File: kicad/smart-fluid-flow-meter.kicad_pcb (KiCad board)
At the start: 2 copper layers, 64 x 54 mm, 14 parts, among them J1 YF-S201, J2 Barrel_Jack, SW1 Factory reset button, U2 ESP32-DevkitV1

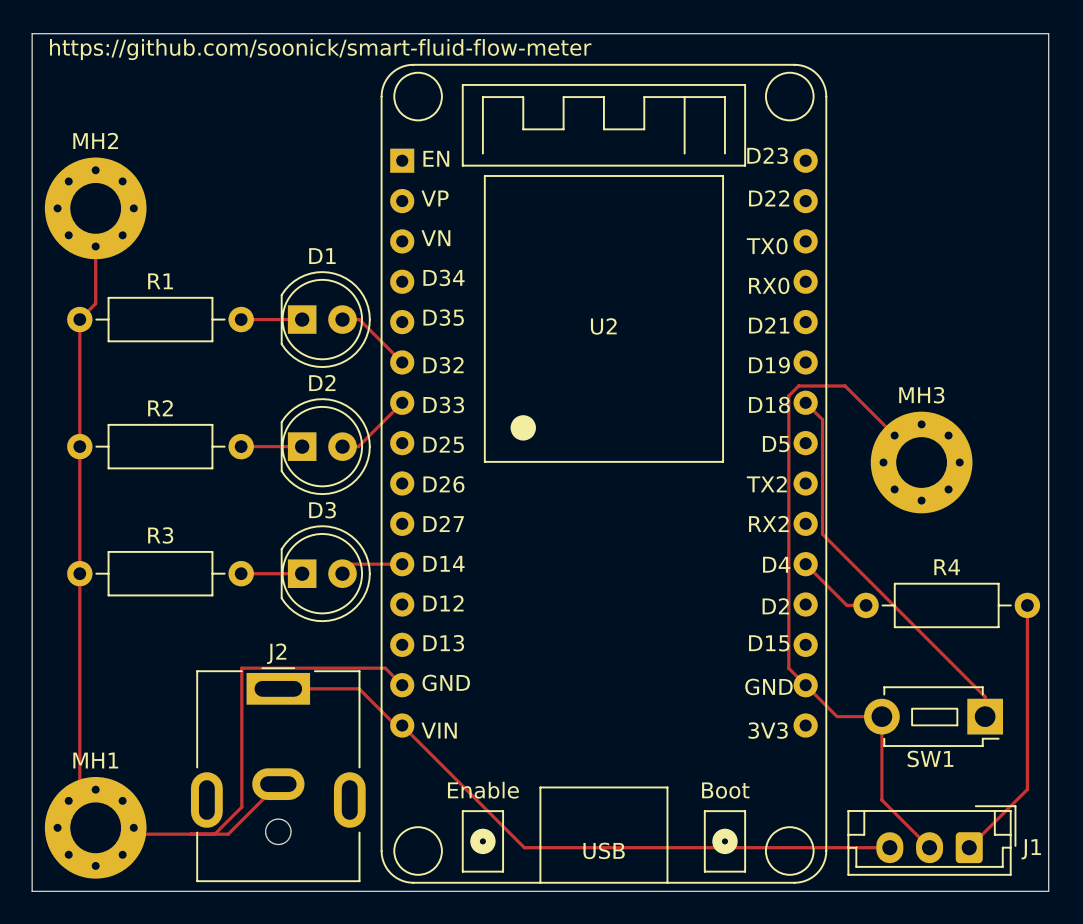
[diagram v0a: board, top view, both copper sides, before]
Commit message: Wider traces and ground plane. #77 (#88)
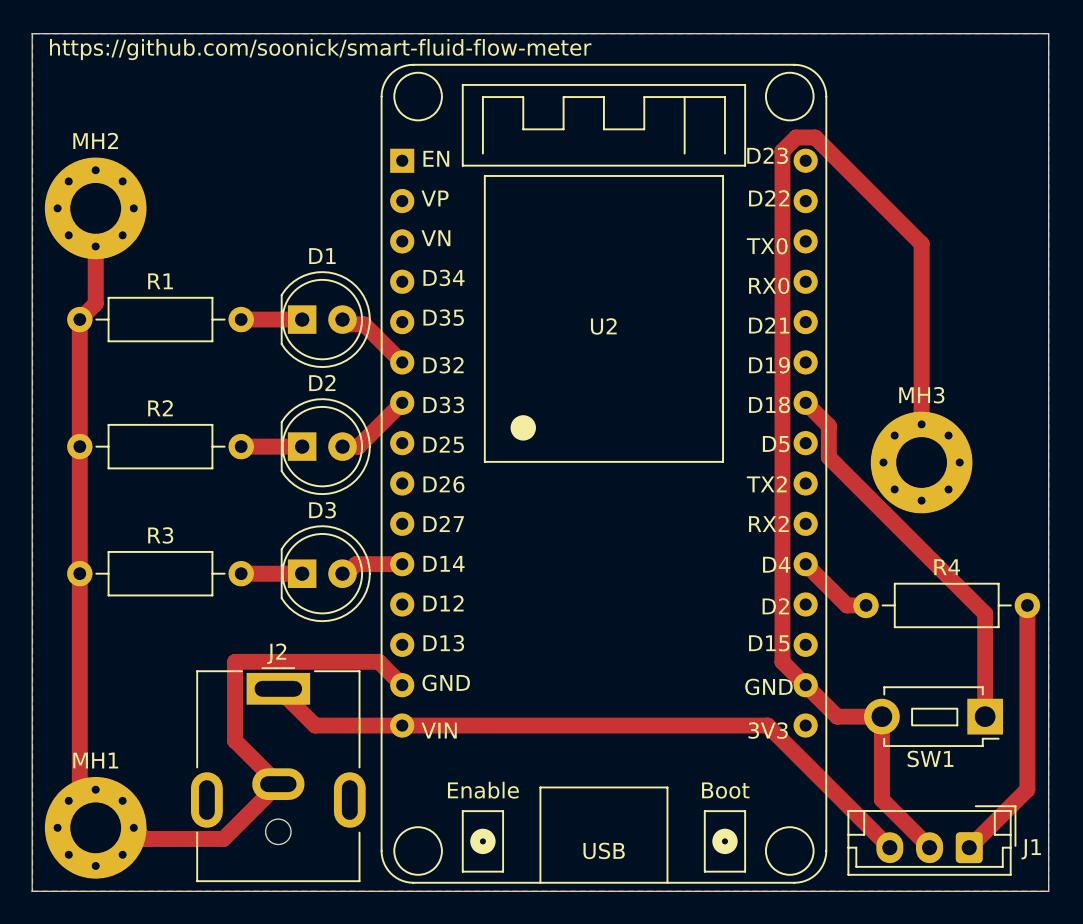
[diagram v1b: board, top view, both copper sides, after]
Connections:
- J1 pad 2: Net-(J1-Pin_2) -> 0
- MH3 pad 1: Net-(J1-Pin_2) -> 0
- SW1 pad 2: Net-(J1-Pin_2) -> 0
- U2 pad 2: Net-(J1-Pin_2) -> 0
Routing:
- net 0: track 73.6 -> 141.4 mm
- net Net-(J1-Pin_2): track 44.4 -> 0.00 mm
- net Net-(D3-A): track 4.01 -> 4.86 mm
- added copper zone on F.Cu, net 0

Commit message: [kicad] Use the gnd plane for gnd connections (#89)
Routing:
- net 0: track 141.4 -> 2.00 mm
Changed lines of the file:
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@@
-	)
-	(segment
-		(start 79.5 89.25)
-		(end 76.05 92.7)
-		(width 1)
-		(layer "F.Cu")
-		(net 1)
-	)
-	(segment
-		(start 111.238 49.394419)
-		(end 112.094419 48.538)
-		(width 1)
-		(layer "F.Cu")
-		(net 1)
-	)
-	(segment
-		(start 120 55.232419)
-		(end 120 66.6)
-		(width 1)
-		(layer "F.Cu")
-		(net 1)
-	)
-	(segment
-		(start 76.8 81.55)
-		(end 76.775 81.575)
-		(width 1)
-		(layer "F.Cu")
-		(net 1)
 	)
 	(segment
@@
 		(end 70.8 92.4)
 		(width 0.2)
-		(layer "F.Cu")
-		(net 1)
-	)
-	(segment
-		(start 85.83 81.55)
-		(end 76.8 81.55)
-		(width 1)
 		(layer "F.Cu")
 		(net 1)
@@
 	)
 	(segment
-		(start 67 60)
-		(end 67 68)
-		(width 1)
-		(layer "F.Cu")
-		(net 1)
-	)
-	(segment
-		(start 112.094419 48.538)
-		(end 113.305581 48.538)
-		(width 1)
-		(layer "F.Cu")
-		(net 1)
-	)
-	(segment
-		(start 113.305581 48.538)
-		(end 120 55.232419)
-		(width 1)
-		(layer "F.Cu")
-		(net 1)
-	)
-	(segment
-		(start 114.68 85)
-		(end 112.7 83.02)
-		(width 1)
-		(layer "F.Cu")
-		(net 1)
-	)
-	(segment
-		(start 117.5 85)
-		(end 114.68 85)
-		(width 1)
-		(layer "F.Cu")
-		(net 1)
-	)
-	(segment
-		(start 76.05 92.7)
-		(end 71.1 92.7)
-		(width 1)
-		(layer "F.Cu")
-		(net 1)
-	)
-	(segment
-		(start 111.238 81.558)
-		(end 111.238 49.394419)
-		(width 1)
-		(layer "F.Cu")
-		(net 1)
-	)
-	(segment
-		(start 68 55.4)
-		(end 68 59)
-		(width 1)
-		(layer "F.Cu")
-		(net 1)
-	)
-	(segment
-		(start 67 76)
-		(end 67 91)
-		(width 1)
-		(layer "F.Cu")
-		(net 1)
-	)
-	(segment
-		(start 71.1 92.7)
-		(end 70.4 92)
-		(width 1)
-		(layer "F.Cu")
-		(net 1)
-	)
-	(segment
-		(start 76.775 81.575)
-		(end 76.775 86.525)
-		(width 1)
-		(layer "F.Cu")
-		(net 1)
-	)
-	(segment
-		(start 76.775 86.525)
-		(end 79.5 89.25)
-		(width 1)
-		(layer "F.Cu")
-		(net 1)
-	)
-	(segment
-		(start 112.7 83.02)
-		(end 111.238 81.558)
-		(width 1)
-		(layer "F.Cu")
-		(net 1)
-	)
-	(segment
-		(start 87.3 83.02)
-		(end 85.83 81.55)
-		(width 1)
-		(layer "F.Cu")
-		(net 1)
-	)
-	(segment
 		(start 67 91)
 		(end 68 92)
@@
 		(layer "F.Cu")
 		(net 1)
-	)
-	(segment
-		(start 67 68)
-		(end 67 76)
-		(width 1)
-		(layer "F.Cu")
-		(net 1)
-	)
-	(segment
-		(start 68 59)
-		(end 67 60)
-		(width 1)
-		(layer "F.Cu")
-		(net 1)
-	)
-	(segment
-		(start 120.5 93.225)
-		(end 117.5 90.225)
-		(width 1)
-		(layer "F.Cu")
-		(net 1)
-	)
-	(segment
-		(start 117.5 90.225)
-		(end 117.5 85)
-		(width 1)
-		(layer "F.Cu")
-		(net 1)
